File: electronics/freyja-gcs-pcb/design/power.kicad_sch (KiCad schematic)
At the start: 122 parts, among them J6 GT-USB-7010ASV, J7 A2543WR-4P-2, J8 XD-PH-10AW, J9 JS350-S02DCA-00, Q1 TM10N06SI, Q2 TM10N06SI, Q3 AO4459, Q4 L2N7002SLLT1G, Q5 L2N7002SLLT1G, Q6 TM10N06SI, Q7 TM10N06SI, Q8 TM10N06SI, SW3 K6-6136D-L1-04, U10 LM74700QDBVRQ1, U11 AMS1117-3.3, U12 RY3730, U3 FM7021DB, U4 CN3702, U5 HY2213-BB3A, U6 HY2213-BB3A, U7 IP2721, U8 SY8368AQQC, U9 LM74700QDBVRQ1

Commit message: cleanup
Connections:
- net MBAT: now reaches BT2.1 (-), BT3.2 (+), BT4.1 (-), BT5.2 (+), C21.2, Q4.2 (S), R22.2, R24.1, R29.1, TP10.1, U5.3 (VSS)
- net BAT- renamed NBAT
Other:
- moved on the sheet: TP1, TP10
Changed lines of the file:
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@@
 	)
 	(junction
-		(at 170.18 246.38)
-		(diameter 0)
-		(color 0 0 0 0)
-	)
-	(junction
 		(at 303.53 146.05)
 		(diameter 0)
@@
 	(wire
 		(pts
-			(xy 170.18 246.38) (xy 170.18 257.81)
-		)
-		(stroke
-			(width 0)
-			(type default)
-		)
-	)
-	(wire
-		(pts
 			(xy 274.32 175.26) (xy 276.86 175.26)
 		)
@@
 	(wire
 		(pts
-			(xy 170.18 241.3) (xy 170.18 246.38)
-		)
-		(stroke
-			(width 0)
-			(type default)
-		)
-	)
-	(wire
-		(pts
 			(xy 148.59 44.45) (xy 148.59 49.53)
 		)
@@
 	(wire
 		(pts
+			(xy 170.18 241.3) (xy 170.18 257.81)
+		)
+		(stroke
+			(width 0)
+			(type default)
+		)
+	)
+	(wire
+		(pts
 			(xy 85.09 132.08) (xy 85.09 134.62)
 		)
@@
 	(wire
 		(pts
-			(xy 170.18 246.38) (xy 173.99 246.38)
+			(xy 170.18 241.3) (xy 177.8 241.3)
 		)
 		(stroke
@@
 	(wire
 		(pts
-			(xy 170.18 232.41) (xy 173.99 232.41)
+			(xy 170.18 232.41) (xy 177.8 232.41)
 		)
 		(stroke
@@
 		)
 	)
-	(label "BAT-"
-		(at 171.45 246.38 0)
+	(label "NBAT"
+		(at 175.26 241.3 0)
+		(effects
+			(font
+				(size 1.27 1.27)
+			)
+			(justify left bottom)
+		)
+	)
+	(label "MBAT"
+		(at 175.26 232.41 0)
 		(effects
 			(font
@@
 	(symbol
 		(lib_id "Connector:TestPoint")
-		(at 173.99 232.41 270)
+		(at 177.8 232.41 270)
 		(unit 1)
 		(exclude_from_sim no)
@@
 		(dnp no)
 		(property "Reference" "TP10"
-			(at 179.324 230.886 0)
+			(at 183.134 230.886 0)
 			(effects
 				(font
@@
 		)
 		(property "Value" "TestPoint"
-			(at 176.0221 234.95 0)
+			(at 179.8321 234.95 0)
 			(effects
 				(font
@@
 		)
 		(property "Footprint" "TestPoint:TestPoint_Pad_D3.0mm"
-			(at 173.99 237.49 0)
+			(at 177.8 237.49 0)
 			(effects
 				(font
@@
 		)
 		(property "Datasheet" "~"
-			(at 173.99 237.49 0)
+			(at 177.8 237.49 0)
 			(effects
 				(font
@@
 		)
 		(property "Description" "test point"
-			(at 173.99 232.41 0)
+			(at 177.8 232.41 0)
 			(effects
 				(font
@@
 	(symbol
 		(lib_id "Connector:TestPoint")
-		(at 173.99 246.38 270)
+		(at 177.8 241.3 270)
 		(unit 1)
 		(exclude_from_sim no)
@@
 		(dnp no)
 		(property "Reference" "TP1"
-			(at 179.324 244.856 0)
+			(at 183.134 239.776 0)
 			(effects
 				(font
@@
 		)
 		(property "Value" "TestPoint"
-			(at 176.0221 248.92 0)
+			(at 179.8321 243.84 0)
 			(effects
 				(font
@@
 		)
 		(property "Footprint" "TestPoint:TestPoint_Pad_D3.0mm"
-			(at 173.99 251.46 0)
+			(at 177.8 246.38 0)
 			(effects
 				(font
@@
 		)
 		(property "Datasheet" "~"
-			(at 173.99 251.46 0)
+			(at 177.8 246.38 0)
 			(effects
 				(font
@@
 		)
 		(property "Description" "test point"
-			(at 173.99 246.38 0)
+			(at 177.8 241.3 0)
 			(effects
 				(font

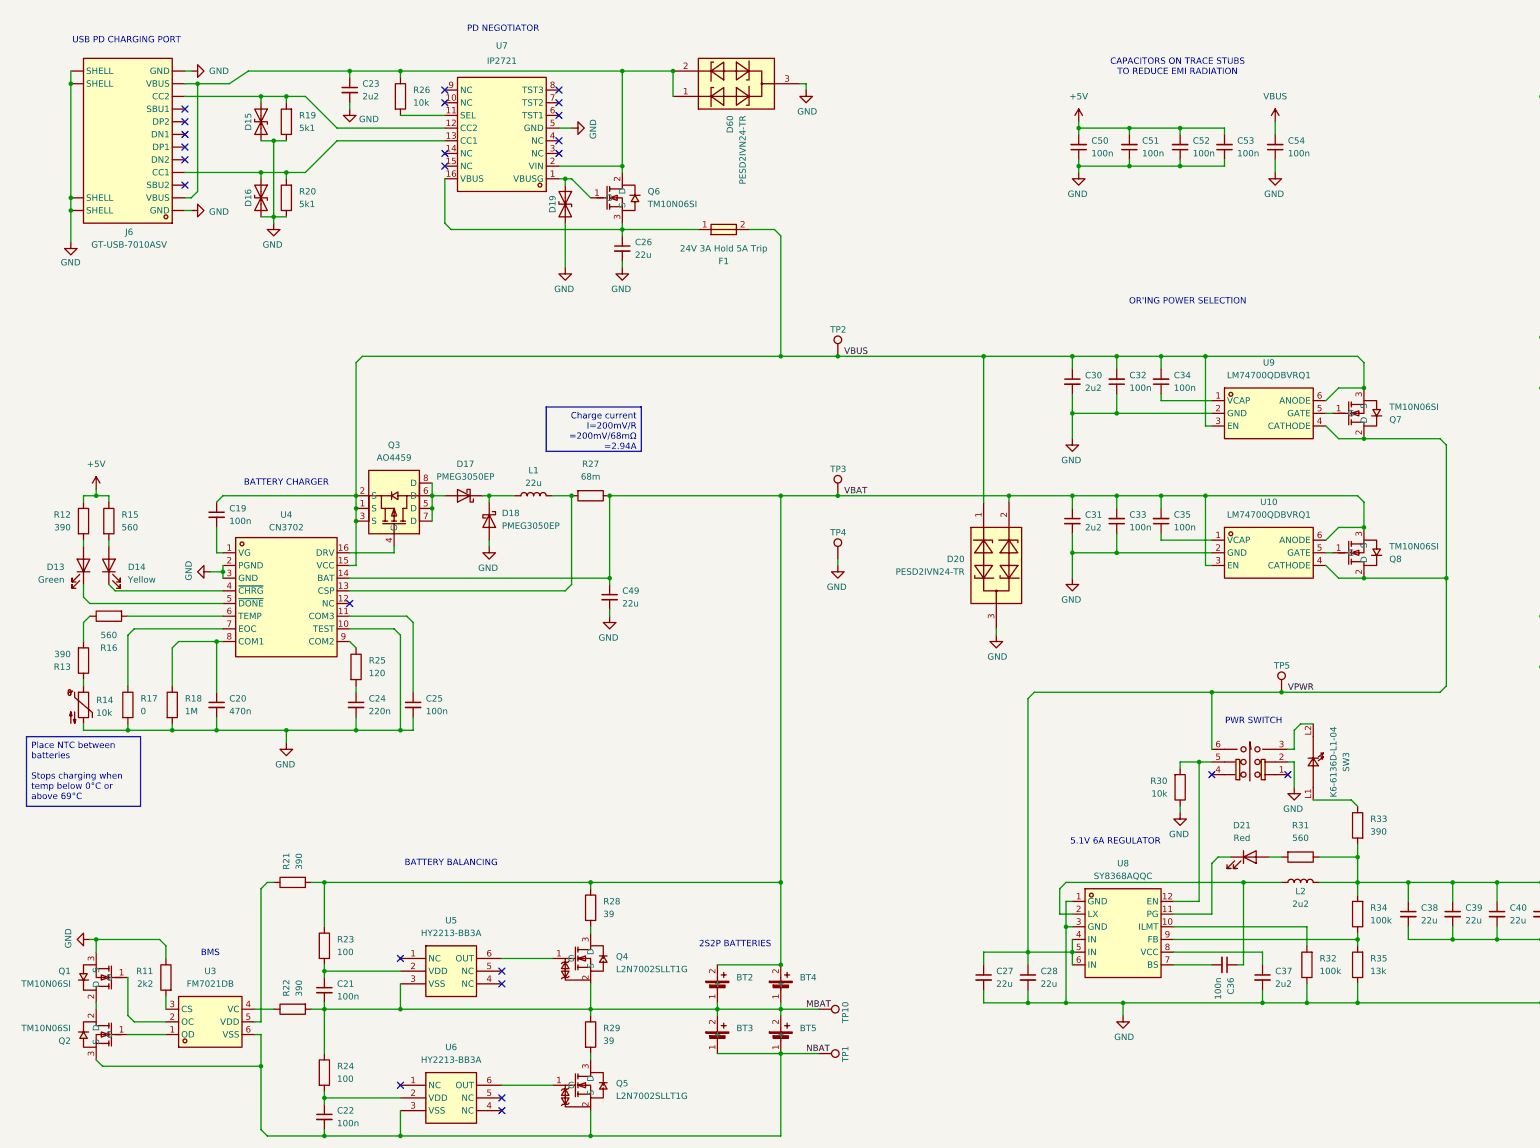
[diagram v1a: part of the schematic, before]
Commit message: change to available parts
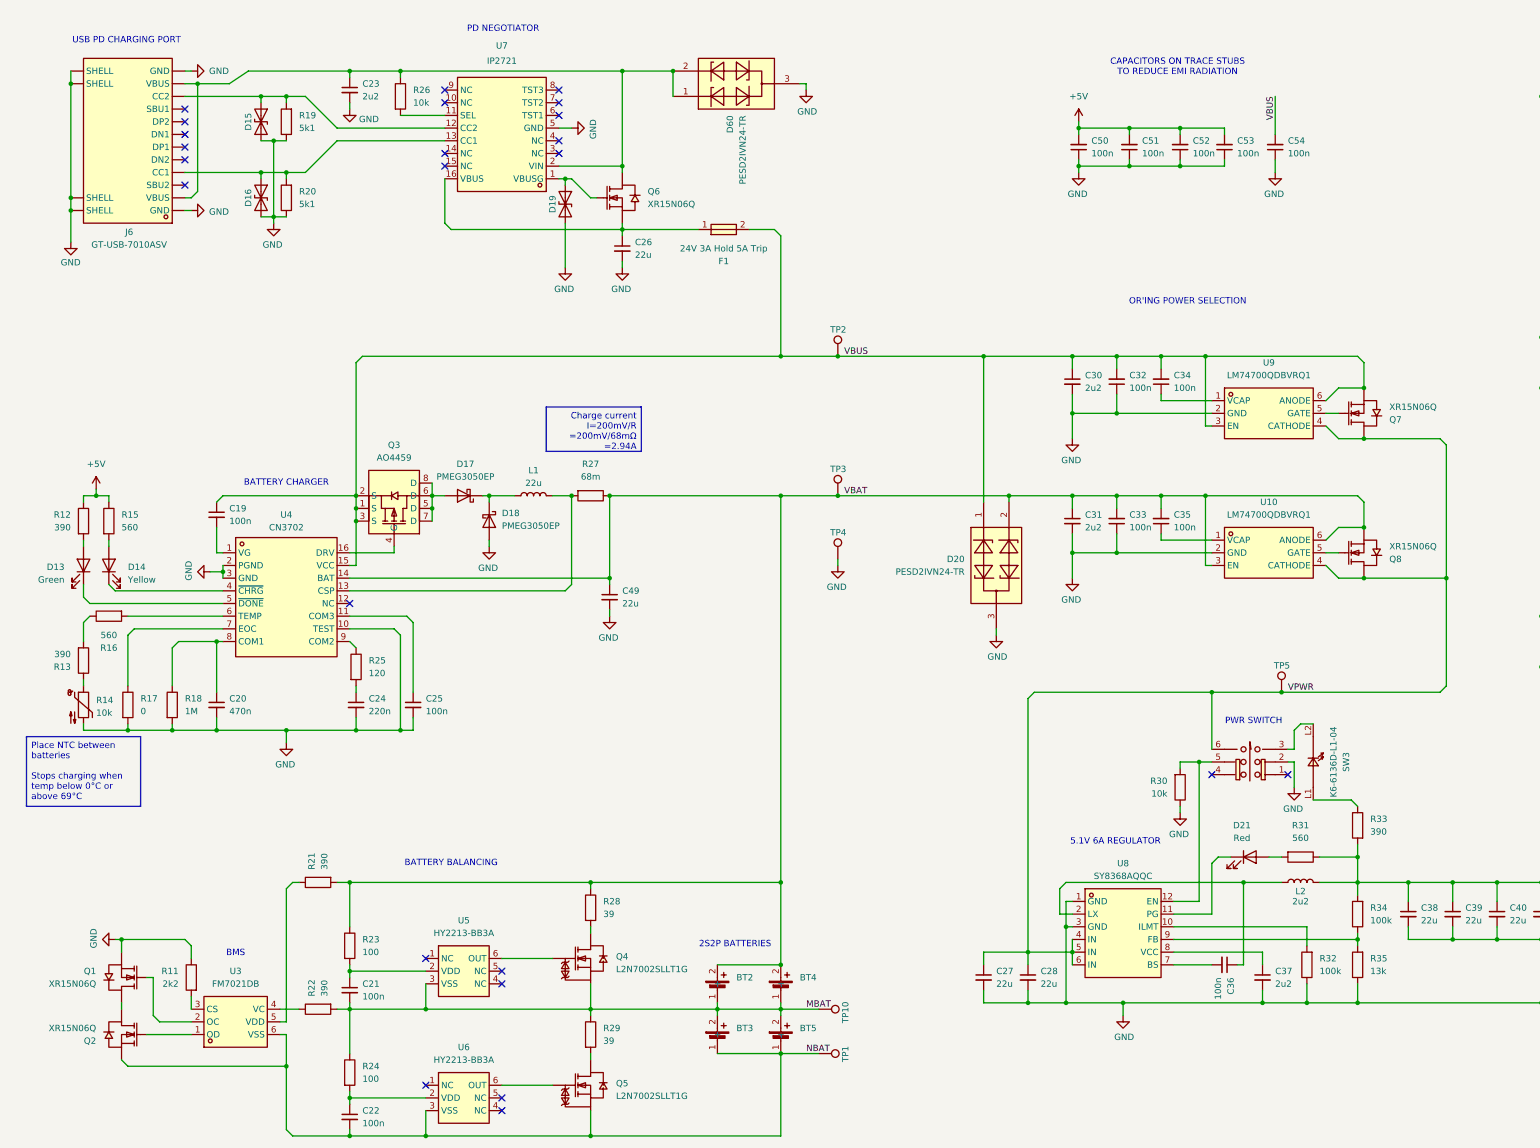
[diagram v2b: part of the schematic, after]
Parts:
- removed L2: 2u2, EasyEDA:IND-SMD_L13.5-W12.8, symbol Device:L
- added L2: 2u2, EasyEDA:IND-SMD_L13.5-W12.6, symbol EasyEDA:MWSA1205S-2R2MT
- J8: symbol EasyEDA:XD-PH-10AW -> EasyEDA:PH-10AW_C2908642; LCSC Part C17700867 -> C2908642
- Q1, Q2, Q6, Q7, Q8: value TM10N06SI -> XR15N06Q; symbol EasyEDA:TM10N06SI -> EasyEDA:XR15N06Q; LCSC Part C7422810 -> C7422896
- R25: LCSC Part C23186 -> C22787
- R27: LCSC Part C154682 -> C419718
- R37: LCSC Part C412428 -> C620833
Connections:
- net +5V: now also L2.2
- net at C36.1, U8.2 (LX): now also L2.1
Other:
- moved on the sheet: C21, C22, R11, R21, R22, R23, R24, U3, U5, U6

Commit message: correct shunt part numbers
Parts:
- R27: LCSC Part C419718 -> C620833
- R37: LCSC Part C620833 -> C46594306
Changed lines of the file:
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@@
 			)
 		)
-		(property "LCSC Part" "C419718"
+		(property "LCSC Part" "C620833"
 			(at 132.08 129.54 90)
 			(effects
@@
 			)
 		)
-		(property "LCSC Part" "C620833"
+		(property "LCSC Part" "C46594306"
 			(at 360.68 118.11 0)
 			(effects
